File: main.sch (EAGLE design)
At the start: 25 parts, among them IC1 STM32F303CBT, IC3 REG1117, IC4 75174PWR, IC5 ULN2801A, IC6 MAX232ECWE

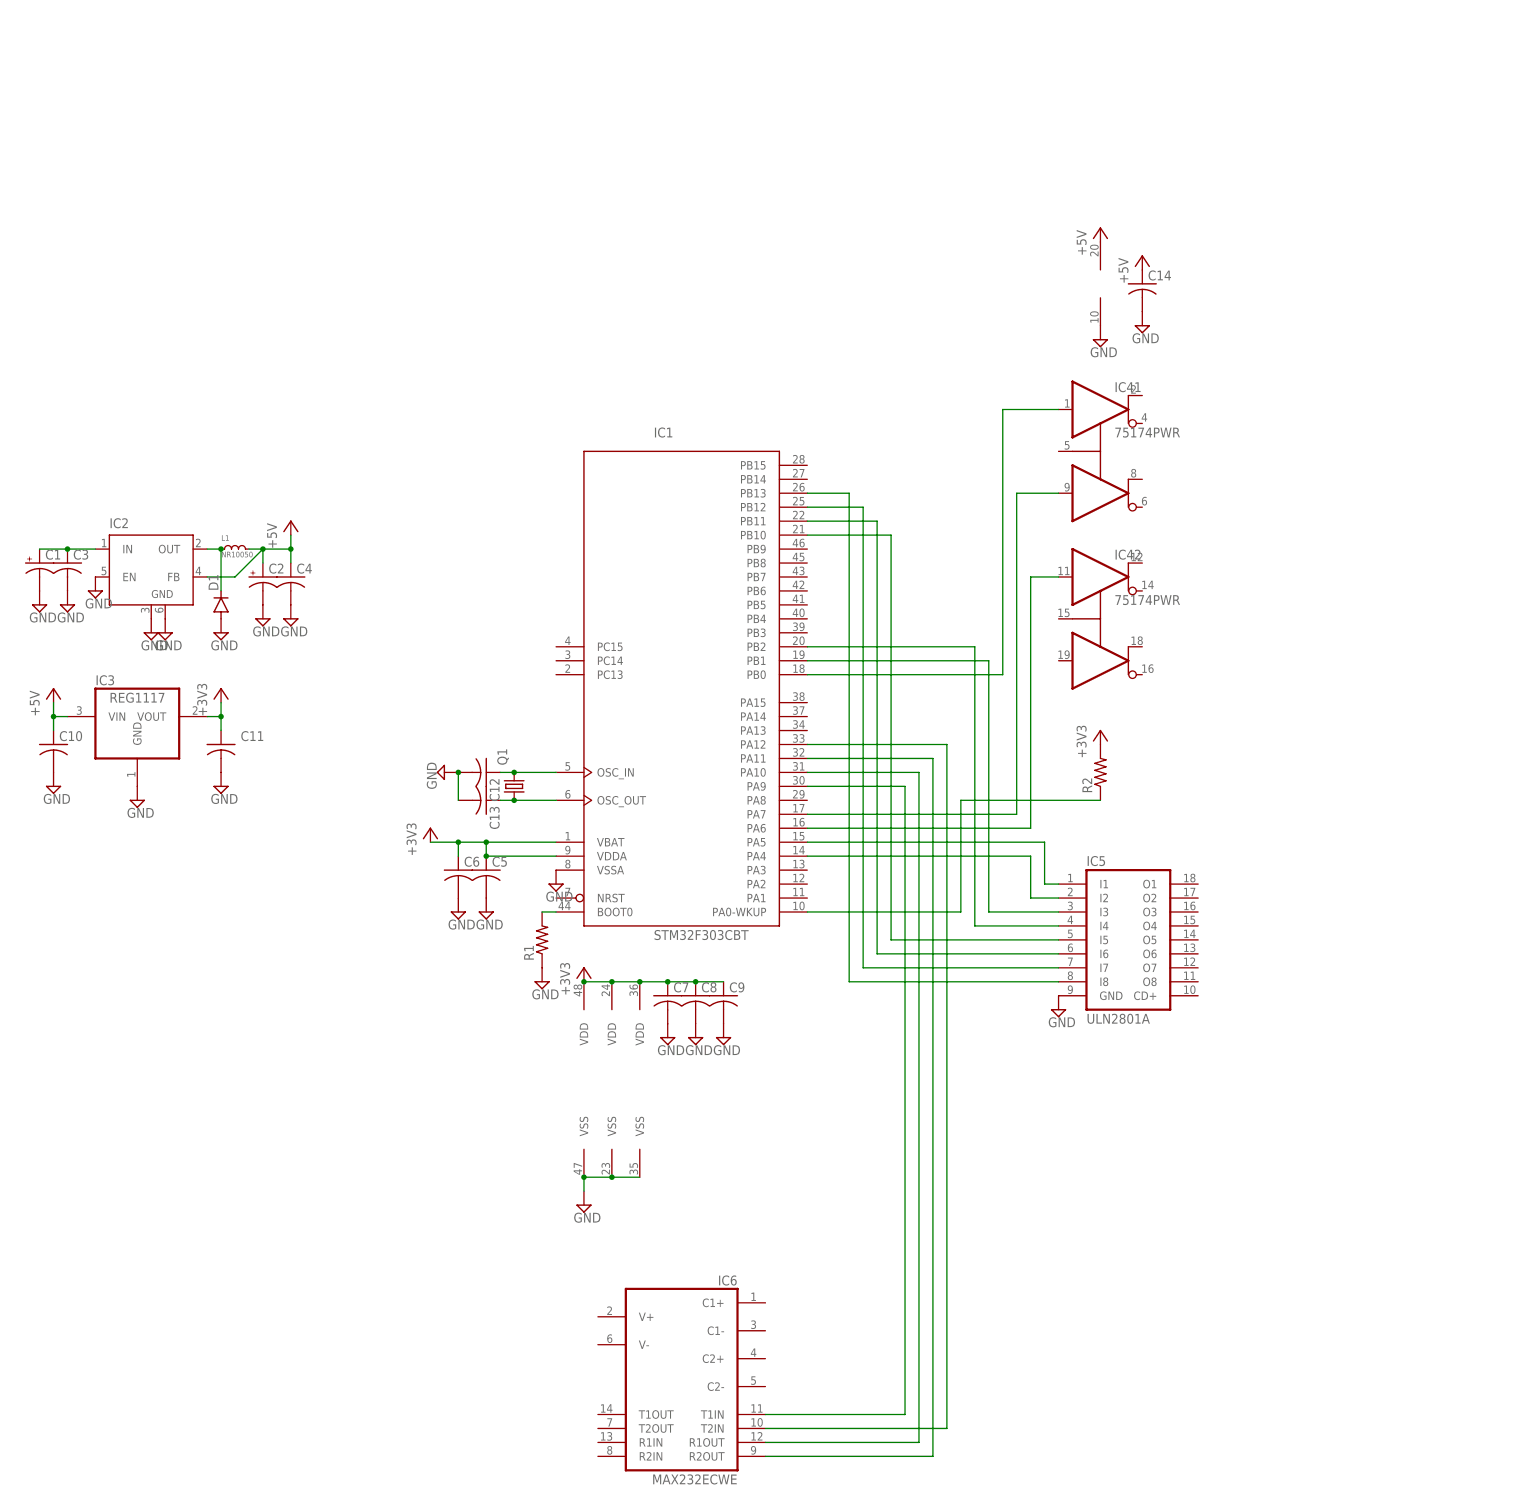
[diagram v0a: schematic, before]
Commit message: Update main.sch
マイコンを変更して，ドライバを追加
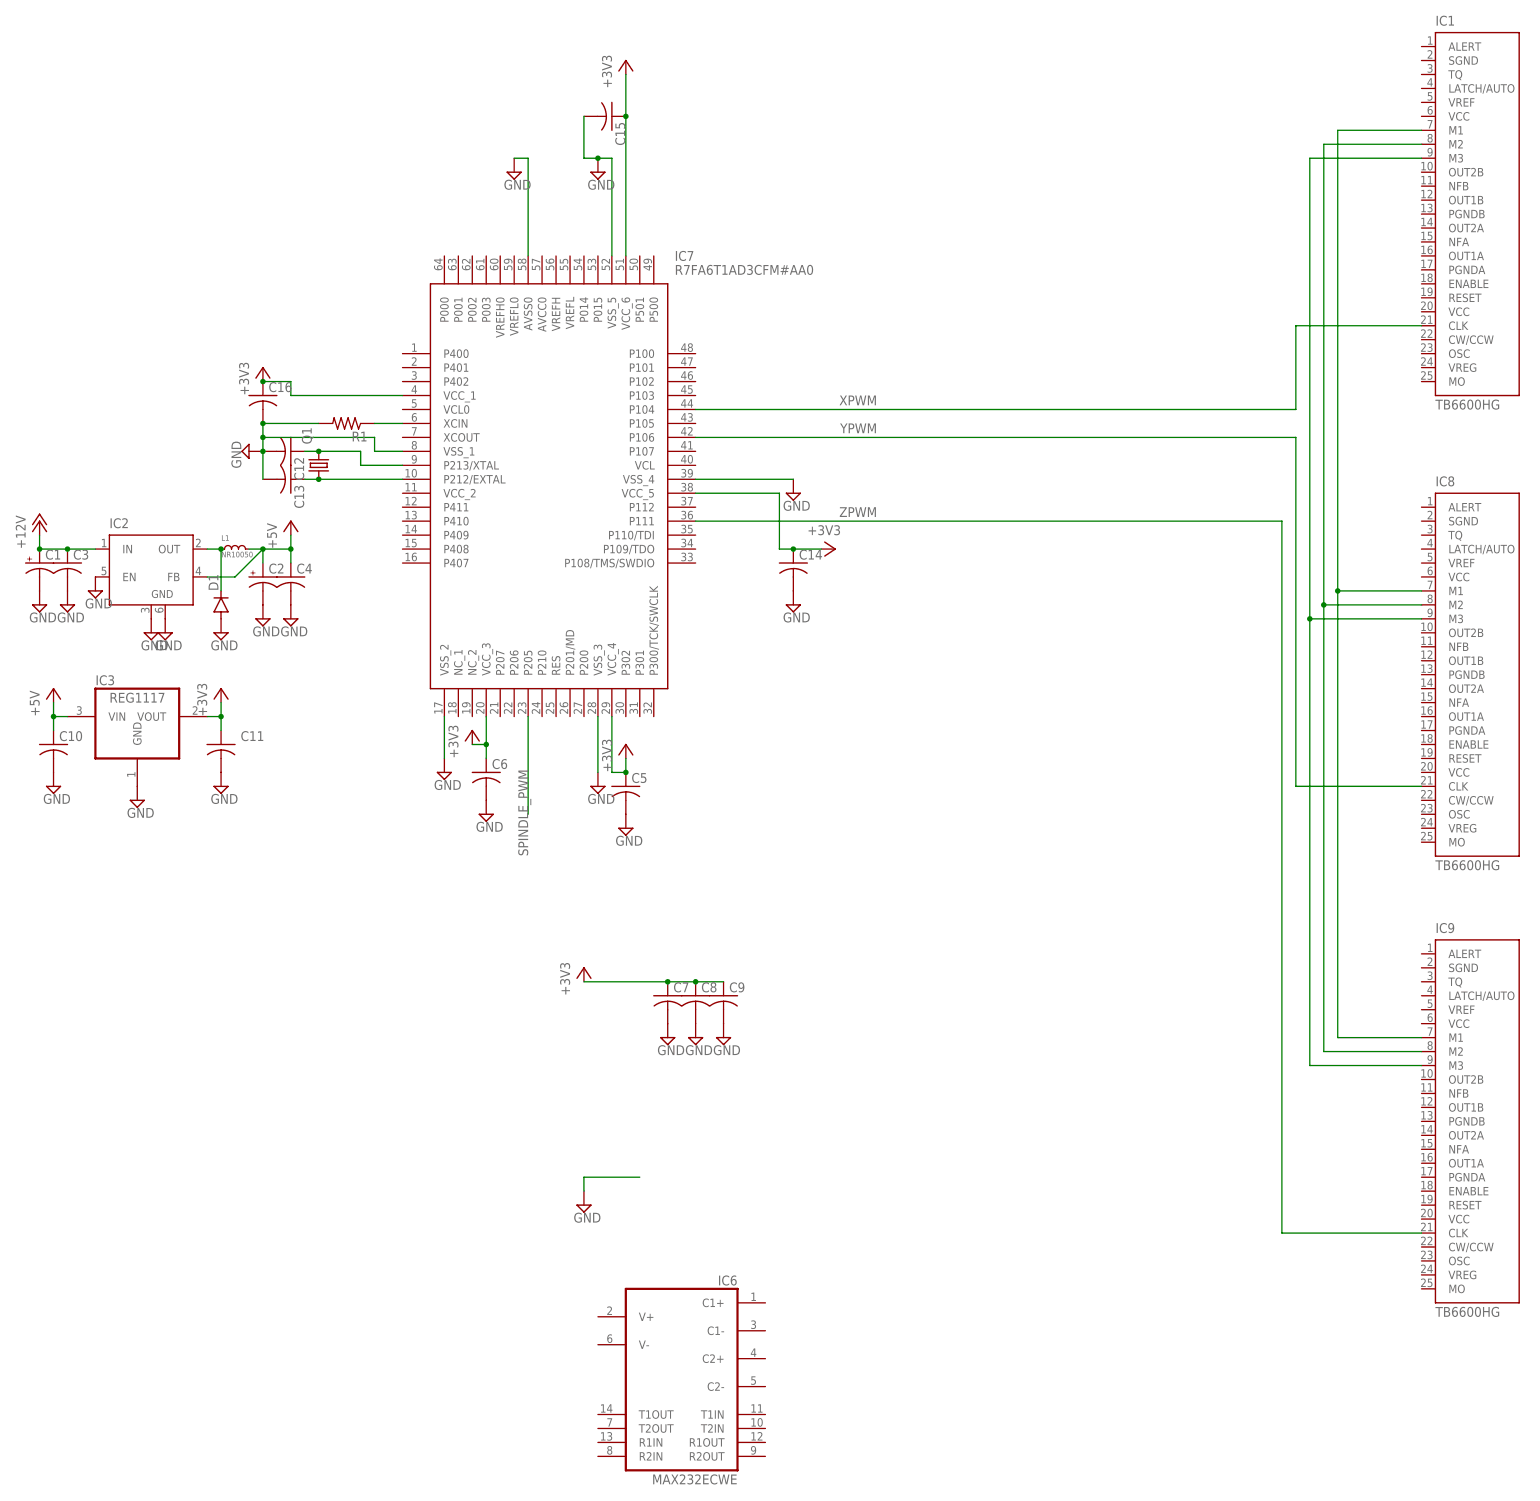
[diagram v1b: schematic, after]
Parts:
- removed IC4: 75174PWR, ti:75174PWR
- removed IC5: ULN2801A, uln-udn:ULN2801A
- removed R2: (no value), rcl:R-US_R0805
- added C15, C16: (no value), rcl:C-USC0603K
- added IC7: R7FA6T1AD3CFM#AA0, renesas:R7FA6T1AD3CFM#AA0
- added IC8, IC9: TB6600HG, toshiba:TB6600HG
- IC1: value STM32F303CBT -> TB6600HG; device micro-stm_v3:STM32F303CBT -> toshiba:TB6600HG
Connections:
- net N$1 renamed +12V
- removed net N$12: IC1MCU.PA11, IC6G$1.R2OUT
- removed net N$13: IC1MCU.PA0-WKUP, R2.1
- removed net N$14: IC1MCU.PA5, IC5.I1
- removed net N$15: IC1MCU.PA4, IC5.I2
- removed net N$16: IC1MCU.PB1, IC5.I3
- removed net N$17: IC1MCU.PB2, IC5.I4
- removed net N$18: IC1MCU.PB10, IC5.I5
- removed net N$19: IC1MCU.PB11, IC5.I6
- removed net N$20: IC1MCU.PB12, IC5.I7
- removed net N$21: IC1MCU.PB13, IC5.I8
- removed net N$4: IC1MCU.PA7, IC41.I2
- removed net N$7: IC1MCU.BOOT0, R1.2
- removed net N$8: IC1MCU.PA6, IC42.I1
- new net SPINDLE_PWM: IC7.P205
- new net XPWM: IC1.CLK, IC7.P104
- new net YPWM: IC7.P106, IC8.CLK
- new net ZPWM: IC7.P111, IC9.CLK
- net +3V3: now also C14.1, C15.1, C16.1, IC7.VCC_1, IC7.VCC_3, IC7.VCC_4, IC7.VCC_5, IC7.VCC_6; no longer IC1MCU.VBAT, IC1MCU.VDDA, IC1PWR.VDD@1, IC1PWR.VDD@2, IC1PWR.VDD@3, R2.2
- net +5V: no longer C14.1, IC4PWR.V+
- net GND: now also C15.2, C16.2, IC7.AVSS0, IC7.VSS_1, IC7.VSS_2, IC7.VSS_3, IC7.VSS_4, IC7.VSS_5, R1.2; no longer IC1MCU.VSSA, IC1PWR.VSS@1, IC1PWR.VSS@2, IC1PWR.VSS@3, IC4PWR.V-, IC5.GND, R1.1
- net N$10: now also IC1.M2, IC8.M2, IC9.M2; no longer IC1MCU.PA10, IC6G$1.R1OUT
- net N$11: now also IC1.M3, IC8.M3, IC9.M3; no longer IC1MCU.PA12, IC6G$1.T2IN
- net N$3: now also IC7.XCIN, R1.1; no longer IC1MCU.PB0, IC41.I1
- net N$5: now also IC7.P213/XTAL; no longer IC1MCU.OSC_IN
- net N$6: now also IC7.P212/EXTAL; no longer IC1MCU.OSC_OUT
- net N$9: now also IC1.M1, IC8.M1, IC9.M1; no longer IC1MCU.PA9, IC6G$1.T1IN
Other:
- moved on the sheet: C12, C13, C14, C5, C6, Q1, R1
